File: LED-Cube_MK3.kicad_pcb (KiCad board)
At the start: 2 copper layers, 50 x 50 mm, 31 parts, among them Q1 2N7002, Q2 2N7002, Q3 2N7002, Q4 2N7002, SW1 SW_Push, SW2 SW_Push, U1 74HC595, U2 74HC595, U3 LED_Cube_5mm_4x4x4

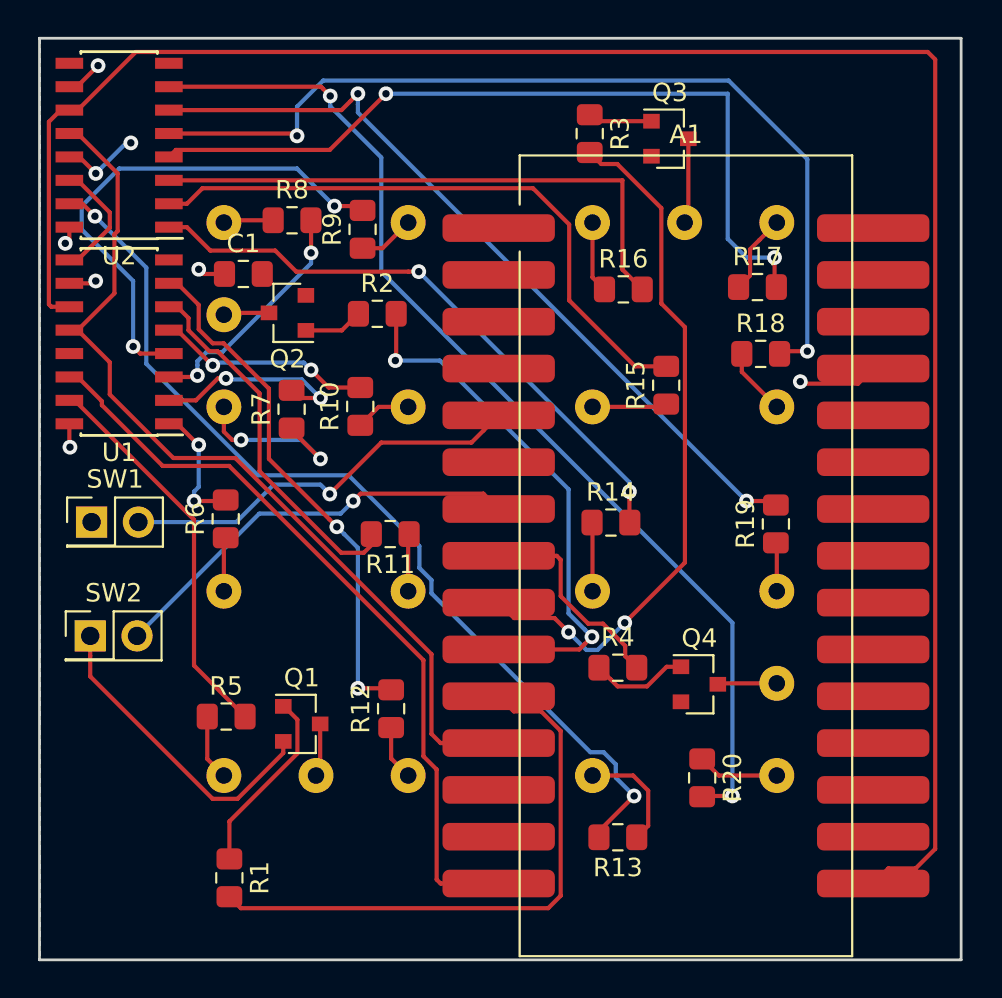
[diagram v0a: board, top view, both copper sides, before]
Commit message: change led spacing to 15mm and add arduino 3d model
Signed-off-by: Thomas Schmid <tom@binary-kitchen.de>
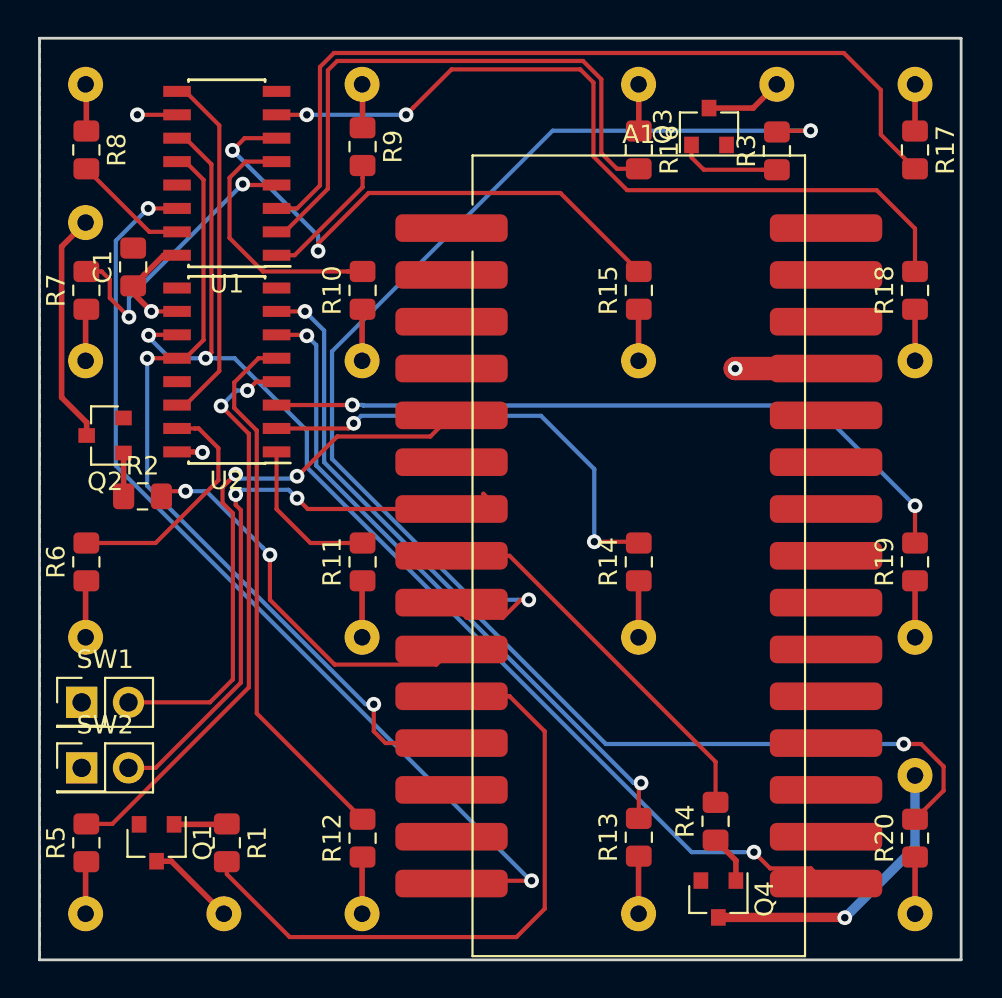
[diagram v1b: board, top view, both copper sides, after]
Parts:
- moved R2 16.1 mm to (25.6, 39.9)
- moved U2 13.5 mm to (30.2, 33.0)
- moved R7 12.9 mm to (22.5, 28.7)
- moved R20 12.0 mm to (67.5, 58.4), turned to 90 degrees
- moved Q2 11.9 mm to (23.6, 36.6)
- moved R8 11.8 mm to (22.5, 21.1), turned to 270 degrees
- moved Q4 11.7 mm to (56.8, 61.7), turned to 270 degrees
- moved R17 11.3 mm to (67.5, 21.1), turned to 270 degrees
- moved U1 10.9 mm to (30.2, 22.3)
- moved R5 10.2 mm to (22.5, 58.6), turned to 90 degrees
- moved R3 10.2 mm to (60.0, 21.1), turned to 90 degrees
- moved Q1 10.2 mm to (26.4, 58.6), turned to 270 degrees
- moved R4 9.88 mm to (56.7, 57.5), turned to 90 degrees
- moved SW1 9.79 mm to (22.3, 51.0)
- moved R18 9.05 mm to (67.5, 28.7), turned to 90 degrees
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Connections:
- net /LED06 renamed LED_6
- net /LED16 renamed LED_16
- net Net-(A1-Pad7) renamed /mode_sw
- R11 pad 2: /LED07 -> LED_10
- R12 pad 2: /LED08 -> LED_14
- R13 pad 2: /LED09 -> LED_15
- R14 pad 2: /LED10 -> LED_11
- R15 pad 2: /LED11 -> LED_7
- R16 pad 2: /LED12 -> LED_3
- R17 pad 2: /LED13 -> LED_4
- R18 pad 2: /LED14 -> LED_8
- R19 pad 2: /LED15 -> LED_12
- R5 pad 2: /LED01 -> LED_13
- R6 pad 2: /LED02 -> LED_9
- R7 pad 2: /LED03 -> LED_5
- R8 pad 2: /LED04 -> LED_1
- R9 pad 2: /LED05 -> LED_2
- U1 pad 1: /LED02 -> LED_2
- U1 pad 15: /LED01 -> LED_1
- U1 pad 2: /LED03 -> LED_3
- U1 pad 3: /LED04 -> LED_4
- U1 pad 4: /LED05 -> LED_5
- U1 pad 6: /LED07 -> LED_7
- U1 pad 7: /LED08 -> LED_8
- U2 pad 1: /LED10 -> LED_10
- U2 pad 15: /LED09 -> LED_9
- U2 pad 2: /LED11 -> LED_11
- U2 pad 3: /LED12 -> LED_12
- U2 pad 4: /LED13 -> LED_13
- U2 pad 5: /LED14 -> LED_14
- U2 pad 6: /LED15 -> LED_15
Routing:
- net /LED09: track 51.6 -> 0.00 mm, vias 2 -> 0
- net /LED14: track 50.6 -> 0.00 mm, vias 2 -> 0
- net LED_4: track 0.00 -> 45.9 mm
- net /LED13: track 44.2 -> 0.00 mm, vias 2 -> 0
- net LED_8: track 0.00 -> 43.9 mm, vias 0 -> 2
- net /LED15: track 43.1 -> 0.00 mm, vias 2 -> 0
- net /scrclk: track 107.9 -> 65.0 mm, vias 0 -> 3
- net LED_12: track 0.00 -> 38.9 mm, vias 0 -> 2
- net LED_15: track 0.00 -> 35.6 mm, vias 0 -> 2
- net /LED11: track 33.7 -> 0.00 mm
- net /LED10: track 32.9 -> 0.00 mm, vias 2 -> 0
- net LED_3: track 0.00 -> 32.0 mm
- net LED_13: track 0.00 -> 31.3 mm, vias 0 -> 2
- net /LED12: track 31.0 -> 0.00 mm
- net LED_7: track 0.00 -> 30.8 mm, vias 0 -> 2
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
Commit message: add 3d model of leds
Signed-off-by: Thomas Schmid <tom@binary-kitchen.de>
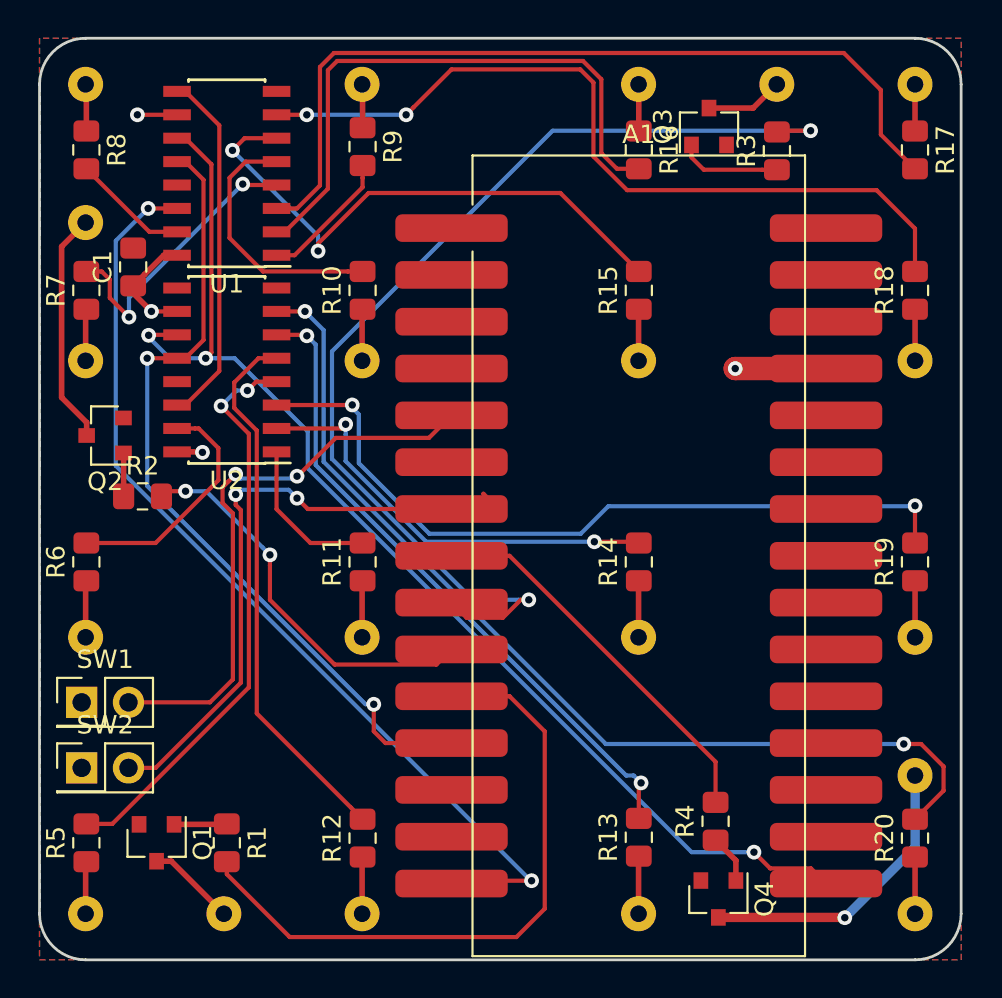
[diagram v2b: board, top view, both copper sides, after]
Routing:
- net LED_12: track 38.9 -> 41.8 mm
- net LED_11: track 25.1 -> 23.6 mm
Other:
- outline, holes or cut-outs redrawn

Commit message: added logo, copyright, name and version
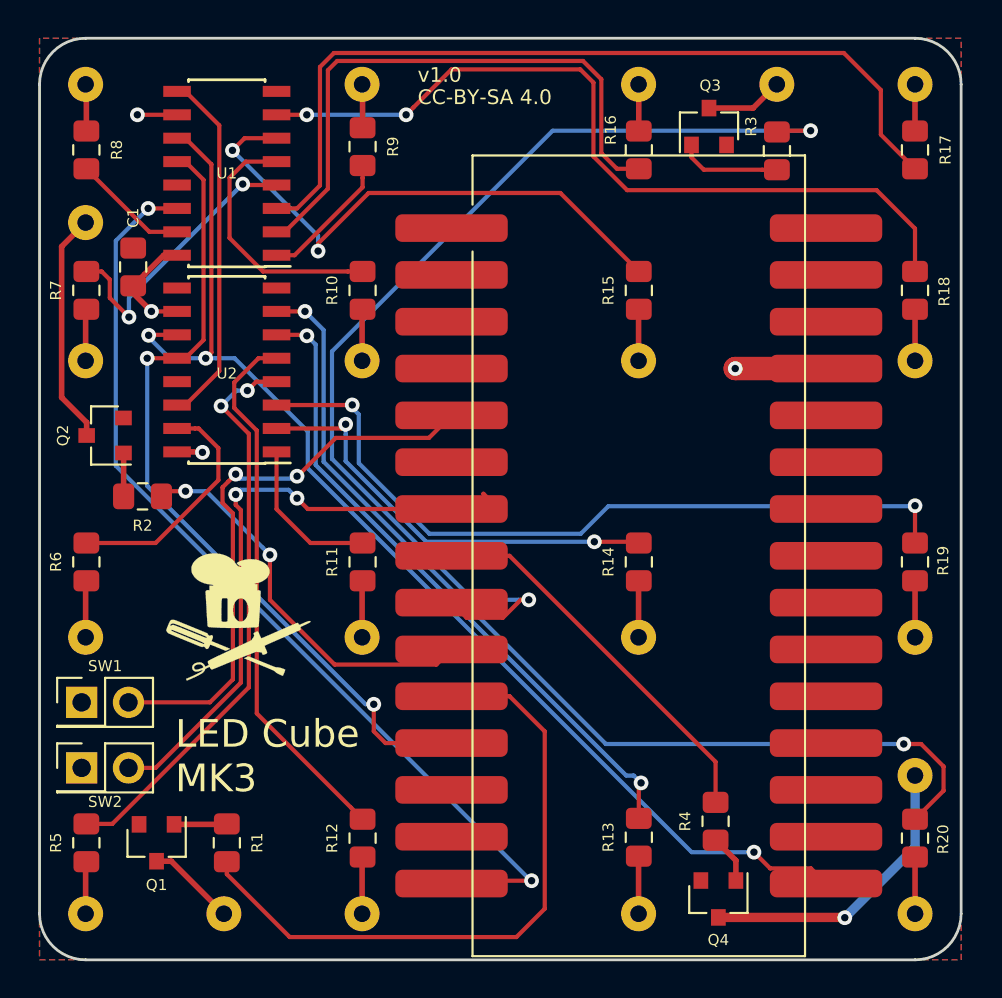
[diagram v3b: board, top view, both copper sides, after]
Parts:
- added G***: Kitchen_LOGO, LED-Cube_MK3:Kitchen_LOGO, F.Cu at (30.8, 46.4)
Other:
- board text added: "CC-BY-SA 4.0"
- board text added: "LED Cube MK3"
- board text added: "v1.0"

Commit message: minor changes
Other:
- board text added: "binary-kitchen.de"
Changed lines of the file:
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@@
   (general
     (thickness 1.6)
-    (drawings 11)
+    (drawings 12)
     (tracks 322)
     (zones 0)
@@
     (visible_elements 7FFFF7FF)
     (pcbplotparams
-      (layerselection 0x010fc_ffffffff)
+      (layerselection 0x010f0_ffffffff)
       (usegerberextensions false)
       (usegerberattributes false)
@@
       (outputformat 1)
       (mirror false)
-      (drillshape 1)
+      (drillshape 0)
       (scaleselection 1)
-      (outputdirectory ""))
+      (outputdirectory "gerber/"))
   )
   (net 0 "")
@@
     )
   )
+  (gr_text binary-kitchen.de (at 28.509 64.1745) (layer F.SilkS)
+    (effects (font (size 0.8 0.8) (thickness 0.15)))
+  )
   (gr_text "CC-BY-SA 4.0" (at 40.5105 18.2005) (layer F.SilkS)
